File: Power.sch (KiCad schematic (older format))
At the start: 12 parts, among them Q1 IRF644, U1 MAX1771

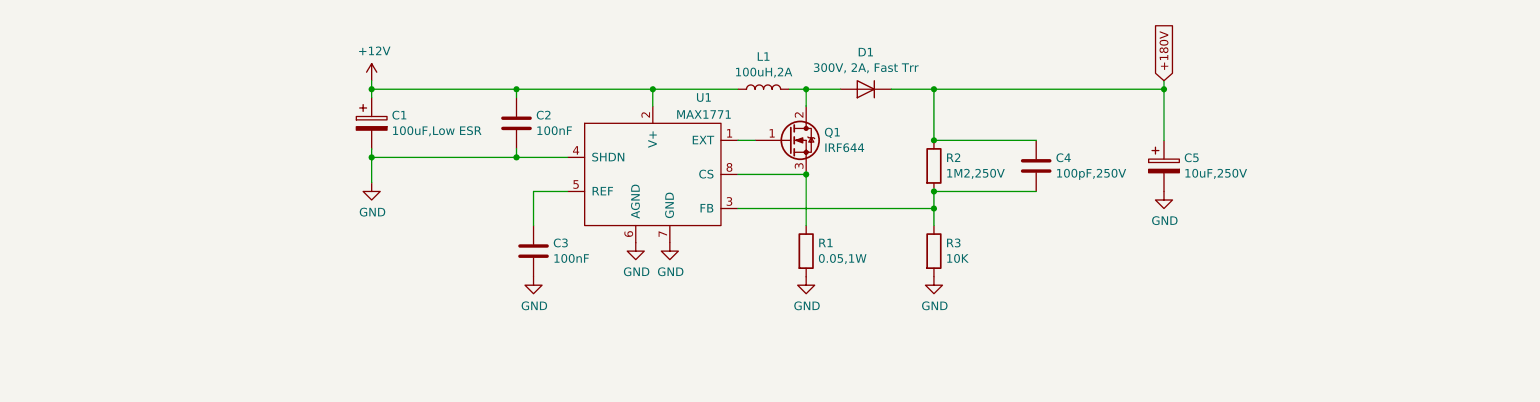
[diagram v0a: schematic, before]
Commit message: Add potentiometer to allow variable output voltage
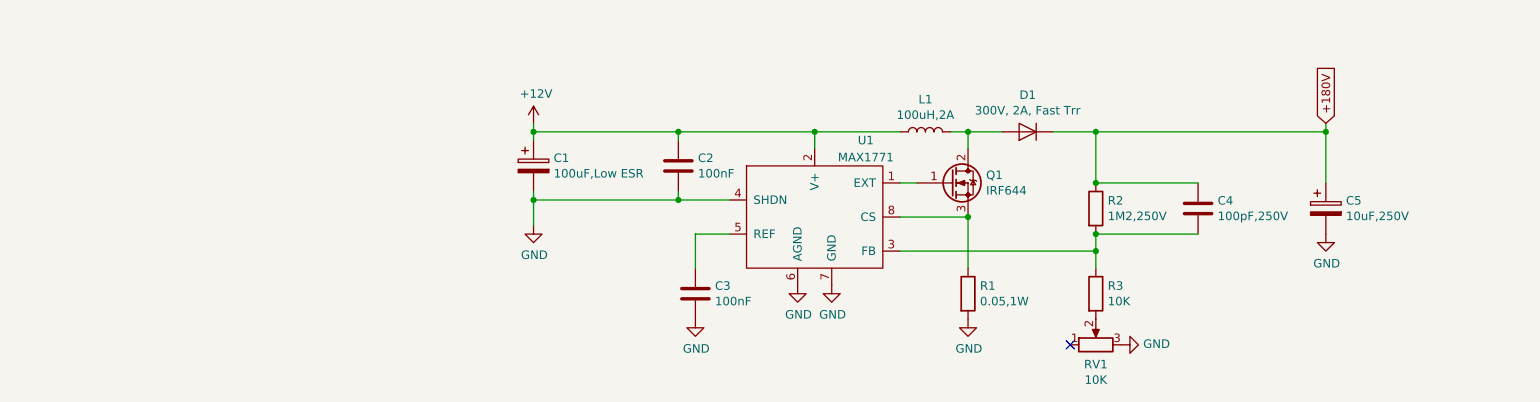
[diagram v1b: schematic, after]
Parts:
- added RV1: 10K, Potentiometer_THT:Potentiometer_Bourns_3339P_Vertical, symbol Device:R_POT
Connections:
- net GND: now also RV1.3; no longer R3.2
- new net: R3.2, RV1.2
- no-connect marks 0 -> 1
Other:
- moved on the sheet: C1, C2, C3, C4, C5, D1, L1, Q1, R1, R2, R3, U1

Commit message: Completed entire board (not tested yet)
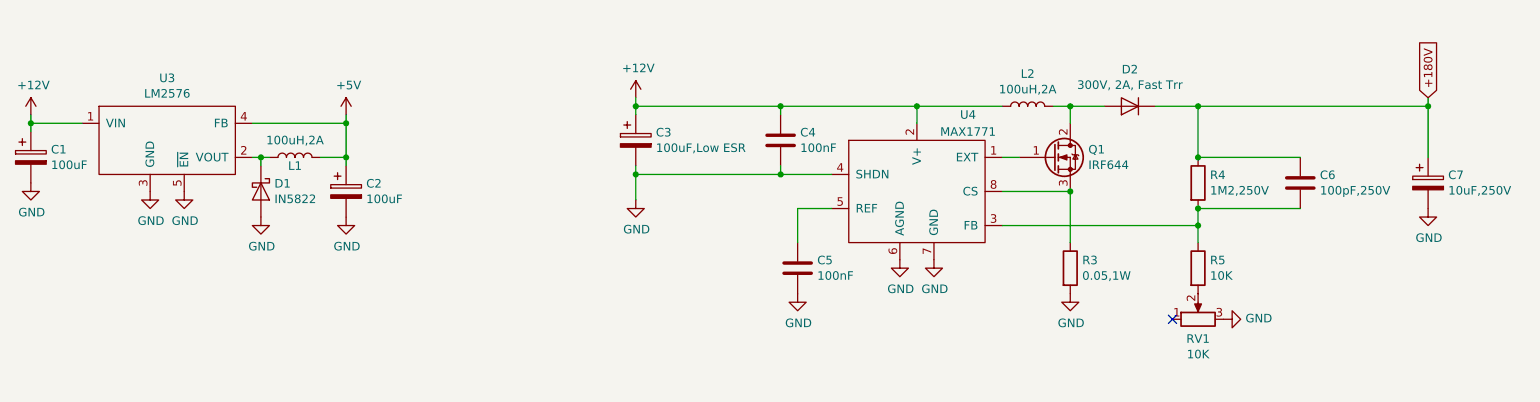
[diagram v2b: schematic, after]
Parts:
- added C1, C2: 100uF, Capacitor_SMD:CP_Elec_6.3x7.7, symbol Device:CP
- added D1: IN5822, Diode_THT:D_DO-201AD_P12.70mm_Horizontal, symbol Device:D_Schottky
- added L1: 100uH,2A, Inductor_SMD:L_12x12mm_H4.5mm, symbol Device:L
- added U3: LM2576, Package_TO_SOT_SMD:TO-263-5_TabPin3, symbol NixieController:LM2576
- renumbered C1 to C3, C2 to C4, C3 to C5, C4 to C6, C5 to C7, D1 to D2, L1 to L2, R1 to R3, R2 to R4, R3 to R5, U1 to U4
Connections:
- net +12V: now also C1.1, U3.1 (VIN)
- net GND: now also C1.2, C2.2, D1.2 (A), U3.3 (GND), U3.5 (~EN)
- new net: D1.1 (K), L1.1, U3.2 (VOUT)
- new net +5V: C2.1, L1.2, U3.4 (FB)
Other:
- moved on the sheet: C3, C4, C5, C6, C7, D2, L2, Q1, R3, R4, R5, RV1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

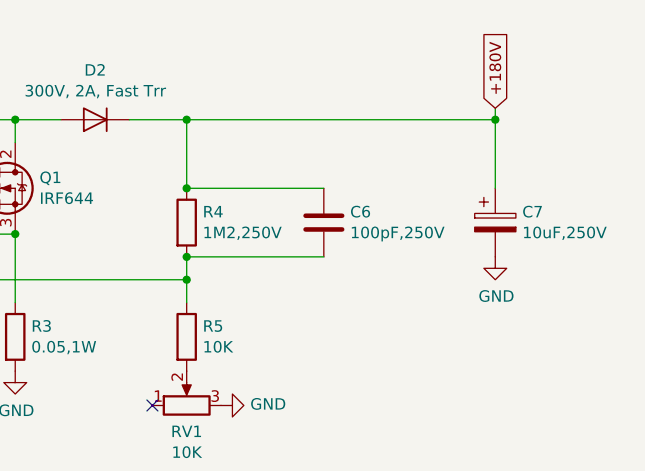
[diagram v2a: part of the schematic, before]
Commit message: Remove feed forward cap for output stabillity
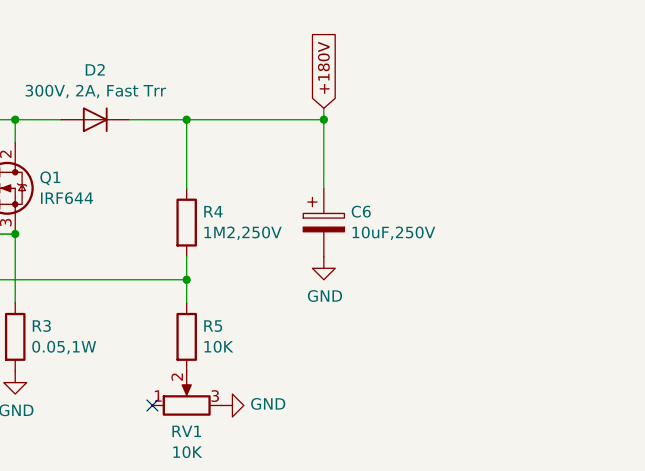
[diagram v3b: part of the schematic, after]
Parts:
- removed C6: 100pF,250V, Capacitor_SMD:C_1206_3216Metric, symbol Device:C
- renumbered C7 to C6
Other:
- moved on the sheet: C6
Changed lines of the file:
@@
 Wire Wire Line
 	5350 3500 5350 3650
-Wire Wire Line
-	10000 3100 10000 3400
 $Comp
 L power:GND #PWR015
 U 1 1 5E9CDFD3
-P 10000 3700
-F 0 "#PWR015" H 10000 3450 50  0001 C CNN
-F 1 "GND" H 10005 3527 50  0000 C CNN
-F 2 "" H 10000 3700 50  0001 C CNN
-F 3 "" H 10000 3700 50  0001 C CNN
-	1    10000 3700
-	1    0    0    -1
-$EndComp
-Text GLabel 10000 3050 1    50   Input ~ 0
+P 9250 3700
+F 0 "#PWR015" H 9250 3450 50  0001 C CNN
+F 1 "GND" H 9255 3527 50  0000 C CNN
+F 2 "" H 9250 3700 50  0001 C CNN
+F 3 "" H 9250 3700 50  0001 C CNN
+	1    9250 3700
+	1    0    0    -1
+$EndComp
+Text GLabel 9250 3050 1    50   Input ~ 0
 +180V
-Wire Wire Line
-	10000 3100 10000 3050
-Connection ~ 10000 3100
 Wire Wire Line
 	8650 3100 8400 3100
@@
 	8100 3100 7900 3100
 Connection ~ 7900 3100
-$Comp
-L Device:C C6
-U 1 1 5E9FDEE9
-P 9250 3550
-F 0 "C6" H 9365 3596 50  0000 L CNN
-F 1 "100pF,250V" H 9365 3505 50  0000 L CNN
-F 2 "Capacitor_SMD:C_1206_3216Metric" H 9288 3400 50  0001 C CNN
-F 3 "~" H 9250 3550 50  0001 C CNN
-	1    9250 3550
-	1    0    0    -1
-$EndComp
-Wire Wire Line
-	8650 3100 10000 3100
-Connection ~ 8650 3100
-Wire Wire Line
-	8650 3400 9250 3400
-Connection ~ 8650 3400
-Wire Wire Line
-	8650 3700 9250 3700
-Connection ~ 8650 3700
 Wire Wire Line
 	5350 3100 6200 3100
@@
 $EndComp
 $Comp
-L Device:CP C7
+L Device:CP C6
 U 1 1 5E9C4E0A
-P 10000 3550
-F 0 "C7" H 10118 3596 50  0000 L CNN
-F 1 "10uF,250V" H 10118 3505 50  0000 L CNN
-F 2 "Capacitor_SMD:CP_Elec_10x10" H 10038 3400 50  0001 C CNN
-F 3 "EEV-EB2E100Q" H 10000 3550 50  0001 C CNN
-	1    10000 3550
+P 9250 3550
+F 0 "C6" H 9368 3596 50  0000 L CNN
+F 1 "10uF,250V" H 9368 3505 50  0000 L CNN
+F 2 "Capacitor_SMD:CP_Elec_10x10" H 9288 3400 50  0001 C CNN
+F 3 "EEV-EB2E100Q" H 9250 3550 50  0001 C CNN
+	1    9250 3550
 	1    0    0    -1
 $EndComp
@@
 Wire Wire Line
 	3650 3150 3650 3200
+Wire Wire Line
+	9250 3050 9250 3100
+Wire Wire Line
+	8650 3100 9250 3100
+Connection ~ 8650 3100
+Connection ~ 9250 3100
+Wire Wire Line
+	9250 3100 9250 3400
 $EndSCHEMATC
